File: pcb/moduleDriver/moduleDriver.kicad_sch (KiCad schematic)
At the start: 32 parts, among them J1 MOTOR, J10 Sensor, J11 Power, J12 Power, J2 MOTOR, J3 MOTOR, J4 MOTOR, J7 Sensor, J8 Sensor, J9 Sensor, U5 PicoW

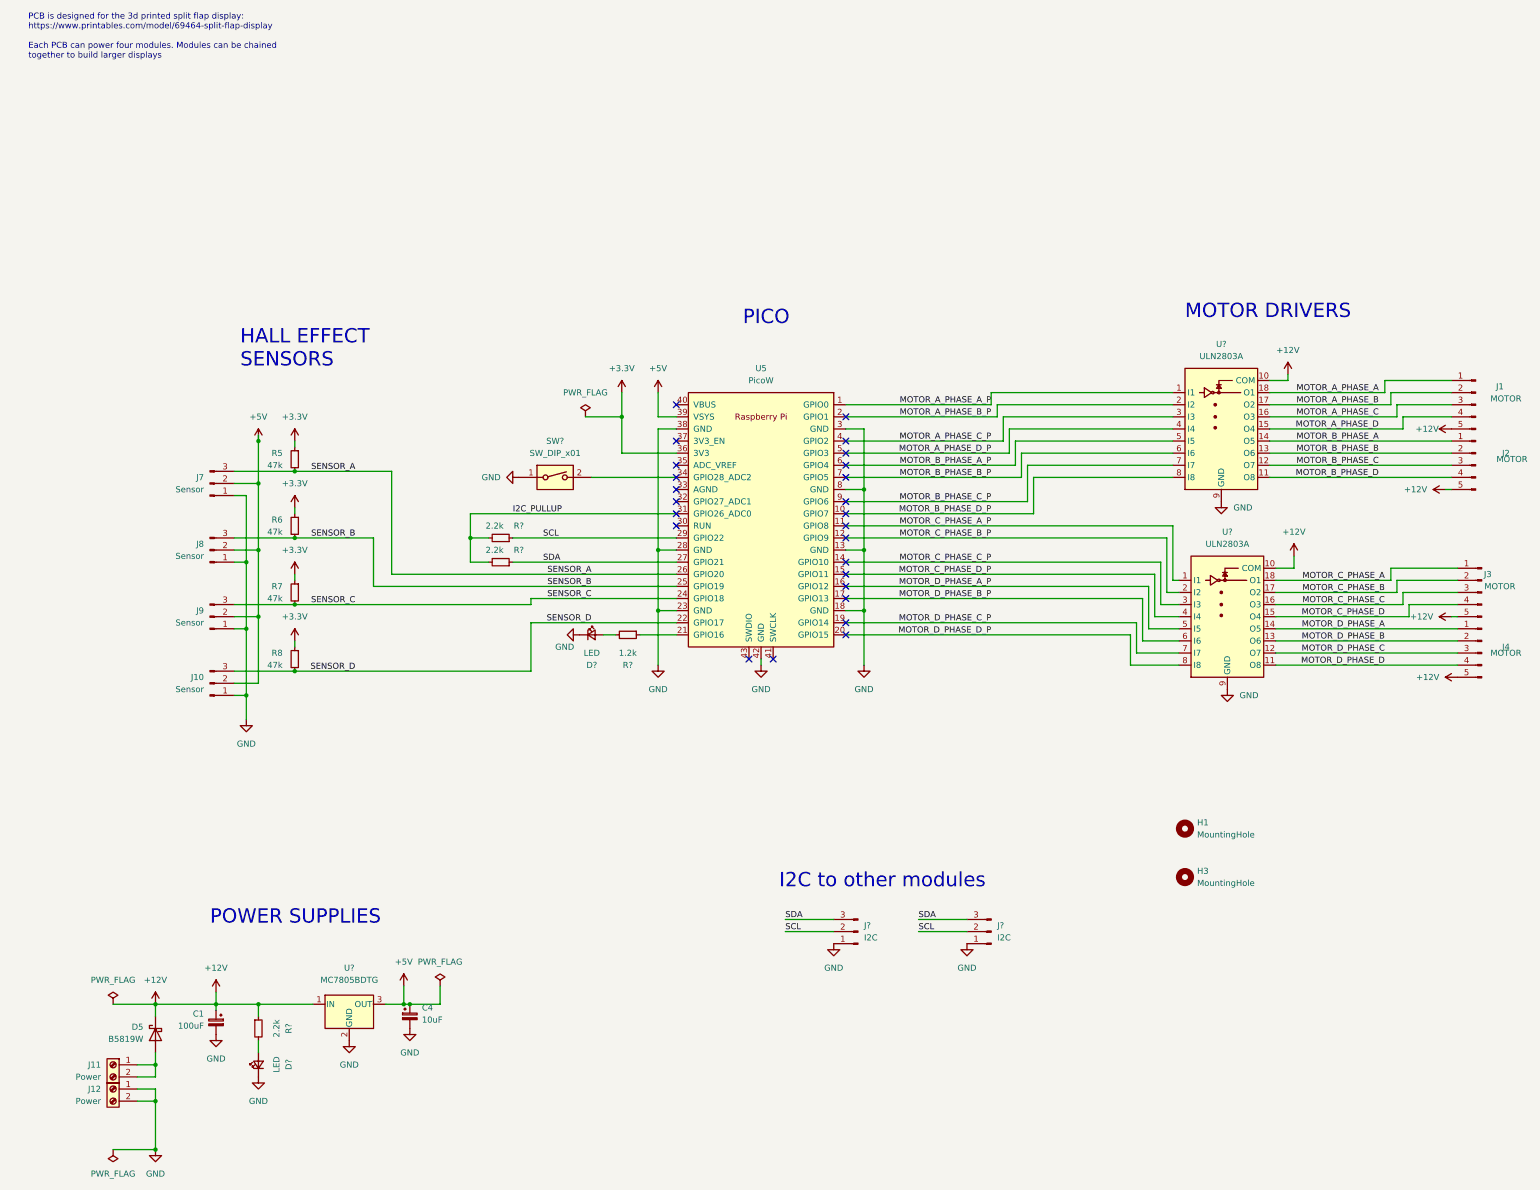
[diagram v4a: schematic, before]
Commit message: cleaned up schematic
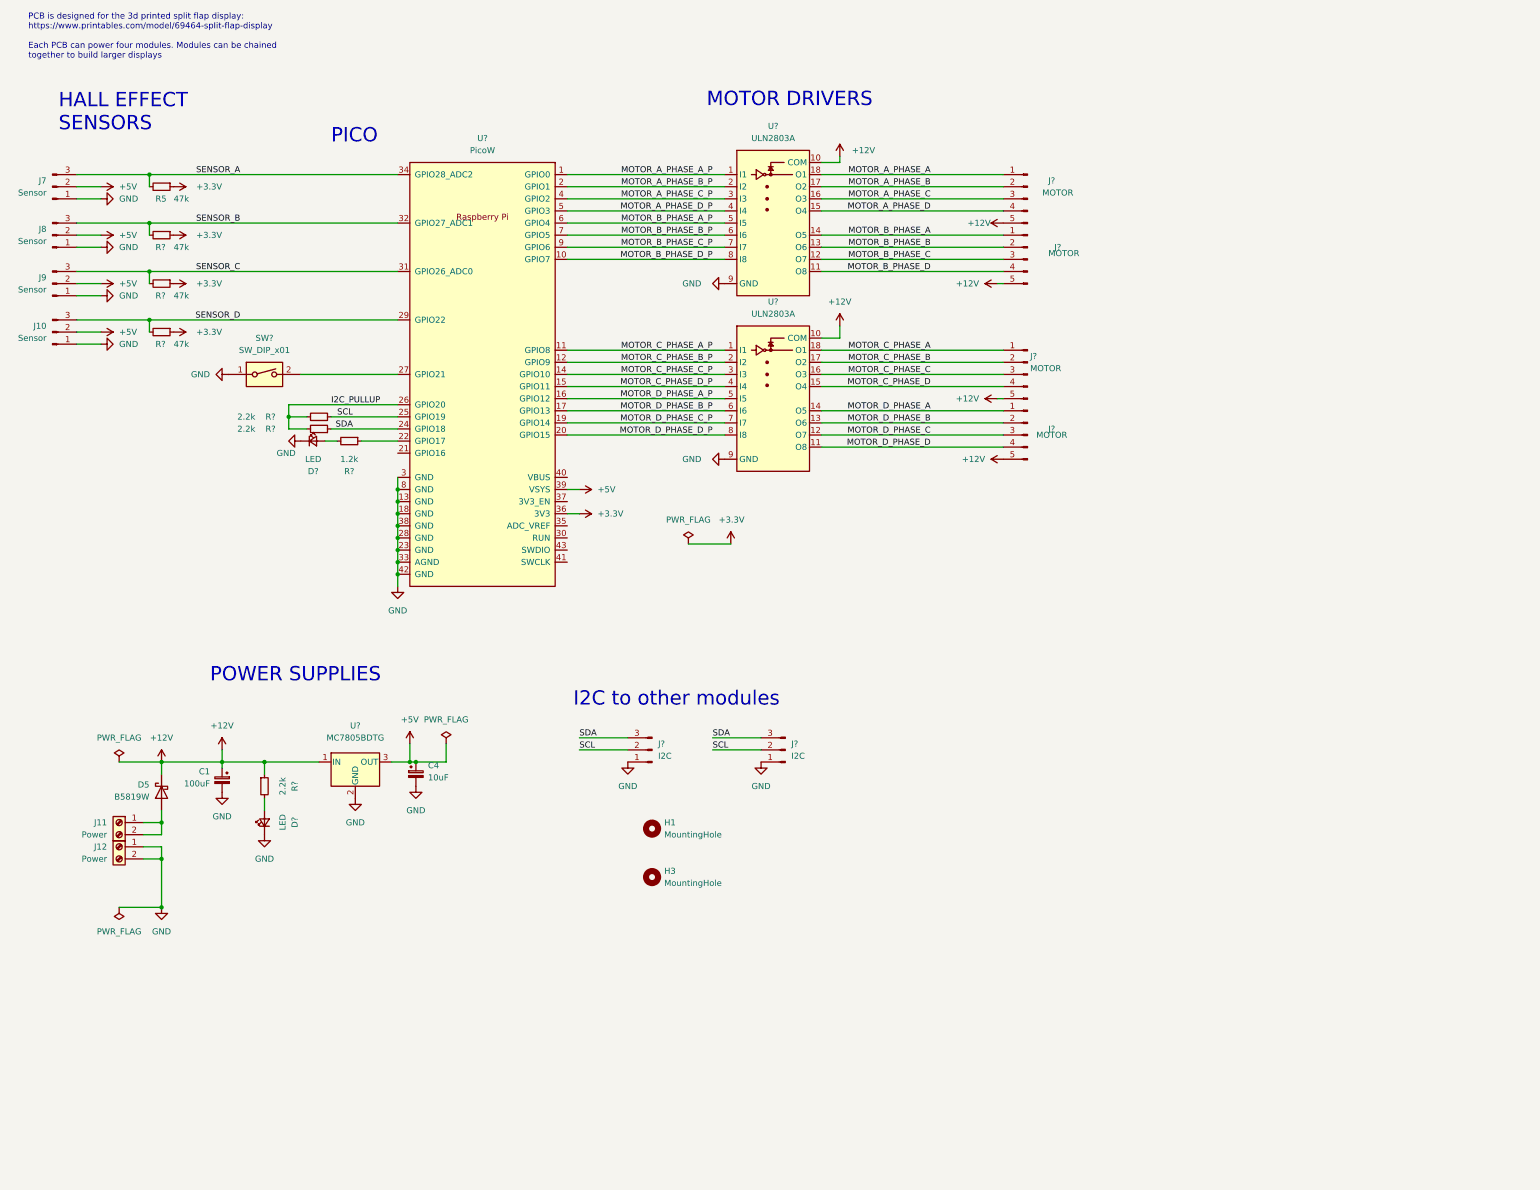
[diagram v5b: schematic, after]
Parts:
- removed J1, J2, J3, J4: MOTOR, Connector_JST:JST_XH_B5B-XH-A_1x05_P2.50mm_Vertical, symbol Connector:Conn_01x05_Male
- removed R6, R7, R8: 47k, Resistor_SMD:R_0603_1608Metric, symbol Device:R_Small
- removed R? (x2): 2.2k, Resistor_SMD:R_0603_1608Metric, symbol Device:R_Small
- removed SW?: SW_DIP_x01, symbol Switch:SW_DIP_x01
- removed U5: PicoW, Library:RPi_PicoW_SMD_TH, symbol RPi_Pico:PicoW
- removed U? (x2): ULN2803A, symbol Transistor_Array:ULN2803A
- added J? (x4): MOTOR, Connector_JST:JST_XH_B5B-XH-A_1x05_P2.50mm_Vertical, symbol Connector:Conn_01x05_Male
- added R? (x2): 2.2k, Resistor_SMD:R_0603_1608Metric, symbol Device:R_Small
- added R? (x3): 47k, Resistor_SMD:R_0603_1608Metric, symbol Device:R_Small
- added SW?: SW_DIP_x01, symbol Switch:SW_DIP_x01
- added U?: PicoW, Library:RPi_PicoW_SMD_TH, symbol RPi_Pico:PicoW
- added U? (x2): ULN2803A, symbol Transistor_Array:ULN2803A
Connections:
- net +12V: now also J?.5 (Pin_5), J?.5 (Pin_5), J?.5 (Pin_5), J?.5 (Pin_5), U?.10 (COM), U?.10 (COM)
- net +3.3V: now also R?.1, R?.1, R?.1, U?.36 (3V3)
- net +5V: now also U?.39 (VSYS)
- net GND: now also SW?.1, U?.13 (GND), U?.18 (GND), U?.23 (GND), U?.28 (GND), U?.3 (GND), U?.33 (AGND), U?.38 (GND), U?.42 (GND), U?.8 (GND), U?.9 (GND), U?.9 (GND)
- net I2C_PULLUP: now also R?.2, R?.2, U?.26 (GPIO20)
- net MOTOR_A_PHASE_A: now also J?.1 (Pin_1), U?.18 (O1)
- net MOTOR_A_PHASE_A_P: now also U?.1 (GPIO0), U?.1 (I1)
- net MOTOR_A_PHASE_B: now also J?.2 (Pin_2), U?.17 (O2)
- net MOTOR_A_PHASE_B_P: now also U?.2 (GPIO1), U?.2 (I2)
- net MOTOR_A_PHASE_C: now also J?.3 (Pin_3), U?.16 (O3)
- net MOTOR_A_PHASE_C_P: now also U?.3 (I3), U?.4 (GPIO2)
- net MOTOR_A_PHASE_D: now also J?.4 (Pin_4), U?.15 (O4)
- net MOTOR_A_PHASE_D_P: now also U?.4 (I4), U?.5 (GPIO3)
- net MOTOR_B_PHASE_A: now also J?.1 (Pin_1), U?.14 (O5)
- net MOTOR_B_PHASE_A_P: now also U?.5 (I5), U?.6 (GPIO4)
- net MOTOR_B_PHASE_B: now also J?.2 (Pin_2), U?.13 (O6)
- net MOTOR_B_PHASE_B_P: now also U?.6 (I6), U?.7 (GPIO5)
- net MOTOR_B_PHASE_C: now also J?.3 (Pin_3), U?.12 (O7)
- net MOTOR_B_PHASE_C_P: now also U?.7 (I7), U?.9 (GPIO6)
- net MOTOR_B_PHASE_D: now also J?.4 (Pin_4), U?.11 (O8)
- net MOTOR_B_PHASE_D_P: now also U?.10 (GPIO7), U?.8 (I8)
- net MOTOR_C_PHASE_A: now also J?.1 (Pin_1), U?.18 (O1)
- net MOTOR_C_PHASE_A_P: now also U?.1 (I1), U?.11 (GPIO8)
- net MOTOR_C_PHASE_B: now also J?.2 (Pin_2), U?.17 (O2)
- net MOTOR_C_PHASE_B_P: now also U?.12 (GPIO9), U?.2 (I2)
- net MOTOR_C_PHASE_C: now also J?.3 (Pin_3), U?.16 (O3)
- net MOTOR_C_PHASE_C_P: now also U?.14 (GPIO10), U?.3 (I3)
- net MOTOR_C_PHASE_D: now also J?.4 (Pin_4), U?.15 (O4)
- net MOTOR_C_PHASE_D_P: now also U?.15 (GPIO11), U?.4 (I4)
- net MOTOR_D_PHASE_A: now also J?.1 (Pin_1), U?.14 (O5)
- net MOTOR_D_PHASE_A_P: now also U?.16 (GPIO12), U?.5 (I5)
- net MOTOR_D_PHASE_B: now also J?.2 (Pin_2), U?.13 (O6)
- net MOTOR_D_PHASE_B_P: now also U?.17 (GPIO13), U?.6 (I6)
- net MOTOR_D_PHASE_C: now also J?.3 (Pin_3), U?.12 (O7)
- net MOTOR_D_PHASE_C_P: now also U?.19 (GPIO14), U?.7 (I7)
- net MOTOR_D_PHASE_D: now also J?.4 (Pin_4), U?.11 (O8)
- net MOTOR_D_PHASE_D_P: now also U?.20 (GPIO15), U?.8 (I8)
- net SCL: now also R?.1, U?.25 (GPIO19)
- net SDA: now also R?.1, U?.24 (GPIO18)
- net SENSOR_A: now also U?.34 (GPIO28_ADC2)
- net SENSOR_B: now also R?.2, U?.32 (GPIO27_ADC1)
- net SENSOR_C: now also R?.2, U?.31 (GPIO26_ADC0)
- net SENSOR_D: now also R?.2, U?.29 (GPIO22)
- net at R?.1: now also U?.22 (GPIO17)
- new net: SW?.2, U?.27 (GPIO21)
- no-connect marks 25 -> 0
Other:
- moved on the sheet: C1, C4, D5, D?, H1, H3, J10, J11, J12, J7, J8, J9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

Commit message: added a couple comments
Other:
- note added: "MASTER SELECT"
- note added: "The switch is to tell which module is the master module. One switch should be ON, and all others OFF. The master module will turn on GPIO20 (I2C_PULLUP), to power the I2C bus. All other modules will have I2C_PULLUP in a High-Z state"
- moved on the sheet: J12
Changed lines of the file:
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@@
   (junction (at 105.41 181.61) (diameter 0) (color 0 0 0 0)
   )
+  (junction (at 53.34 204.47) (diameter 0) (color 0 0 0 0)
+  )
   (junction (at 106.68 181.61) (diameter 0) (color 0 0 0 0)
   )
@@
   (junction (at 102.87 134.62) (diameter 0) (color 0 0 0 0)
   )
-  (junction (at 53.34 201.93) (diameter 0) (color 0 0 0 0)
-  )
   (wire (pts (xy 90.17 114.3) (xy 87.63 114.3))
     (stroke (width 0) (type default) (color 0 0 0 0))
@@
     (stroke (width 0) (type default) (color 0 0 0 0))
   )
-  (wire (pts (xy 53.34 199.39) (xy 53.34 201.93))
-    (stroke (width 0) (type default) (color 0 0 0 0))
-  )
   (wire (pts (xy 80.01 106.68) (xy 102.87 106.68))
     (stroke (width 0) (type default) (color 0 0 0 0))
@@
     (stroke (width 0) (type default) (color 0 0 0 0))
   )
+  (wire (pts (xy 53.34 204.47) (xy 53.34 212.09))
+    (stroke (width 0) (type default) (color 0 0 0 0))
+  )
   (wire (pts (xy 191.77 76.2) (xy 229.87 76.2))
     (stroke (width 0) (type default) (color 0 0 0 0))
@@
     (stroke (width 0) (type default) (color 0 0 0 0))
   )
-  (wire (pts (xy 53.34 201.93) (xy 53.34 212.09))
-    (stroke (width 0) (type default) (color 0 0 0 0))
-  )
   (wire (pts (xy 88.9 111.76) (xy 102.87 111.76))
     (stroke (width 0) (type default) (color 0 0 0 0))
@@
     (stroke (width 0) (type default) (color 0 0 0 0))
   )
-  (wire (pts (xy 53.34 201.93) (xy 49.53 201.93))
+  (wire (pts (xy 53.34 204.47) (xy 49.53 204.47))
     (stroke (width 0) (type default) (color 0 0 0 0))
   )
@@
     (stroke (width 0) (type default) (color 0 0 0 0))
   )
-  (wire (pts (xy 49.53 199.39) (xy 53.34 199.39))
+  (wire (pts (xy 49.53 201.93) (xy 53.34 201.93))
+    (stroke (width 0) (type default) (color 0 0 0 0))
+  )
+  (wire (pts (xy 53.34 204.47) (xy 53.34 201.93))
     (stroke (width 0) (type default) (color 0 0 0 0))
   )
@@
   (wire (pts (xy 35.56 73.66) (xy 40.64 73.66))
     (stroke (width 0) (type default) (color 0 0 0 0))
+  )
+  (text "The switch is to tell which module\nis the master module. One switch\nshould be ON, and all others OFF.\n\nThe master module will turn on GPIO20\n(I2C_PULLUP), to power the I2C bus.  \nAll other modules will have I2C_PULLUP\nin a High-Z state"
+    (at 24.13 119.38 0)
+    (effects (font (size 1.27 1.27)) (justify left bottom))
   )
   (text "HALL EFFECT\nSENSORS" (at 31.75 49.53 0)
@@
   )
   (text "PICO" (at 88.9 52.07 0)
+    (effects (font (size 3 3)) (justify left bottom))
+  )
+  (text "MASTER SELECT" (at 24.13 101.6 0)
     (effects (font (size 3 3)) (justify left bottom))
   )
@@
     (pin "1")
   )
-  (symbol (lib_id "Connector:Screw_Terminal_01x02") (at 44.45 199.39 0) (mirror y) (unit 1)
-    (in_bom yes) (on_board yes) (fields_autoplaced)
-    (property "Reference" "J12" (id 0) (at 41.91 199.3899 0)
+  (symbol (lib_id "Connector:Screw_Terminal_01x02") (at 44.45 201.93 0) (mirror y) (unit 1)
+    (in_bom yes) (on_board yes) (fields_autoplaced)
+    (property "Reference" "J12" (id 0) (at 41.91 201.9299 0)
       (effects (font (size 1.27 1.27)) (justify left))
     )
-    (property "Value" "Power" (id 1) (at 41.91 201.9299 0)
+    (property "Value" "Power" (id 1) (at 41.91 204.4699 0)
       (effects (font (size 1.27 1.27)) (justify left))
     )
-    (property "Footprint" "Library:ScrewTerminal-5.08-2P" (id 2) (at 44.45 199.39 0)
-      (effects (font (size 1.27 1.27)) hide)
-    )
-    (property "Datasheet" "~" (id 3) (at 44.45 199.39 0)
-      (effects (font (size 1.27 1.27)) hide)
-    )
-    (property "Comment" "-" (id 4) (at 44.45 199.39 0)
-      (effects (font (size 1.27 1.27)) hide)
-    )
+    (property "Footprint" "Library:ScrewTerminal-5.08-2P" (id 2) (at 44.45 201.93 0)
+      (effects (font (size 1.27 1.27)) hide)
+    )
+    (property "Datasheet" "~" (id 3) (at 44.45 201.93 0)
+      (effects (font (size 1.27 1.27)) hide)
+    )
+    (property "Comment" "-" (id 4) (at 44.45 201.93 0)
+      (effects (font (size 1.27 1.27)) hide)
+    )

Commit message: update more text
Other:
- note added: "As you're laying out, double click the pico and click edit symbol. Then swap around all the GPIOs to make routing easier. Except for the I2C bus, literally all the GPIOS are interchangeable. Make routing simple."
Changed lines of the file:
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@@
     (effects (font (size 3 3)) (justify left bottom))
+  )
+  (text "As you're laying out, double click the pico and click\nedit symbol.  Then swap around all the GPIOs to make \nrouting easier.  Except for the I2C bus, literally\nall the GPIOS are interchangeable.  Make routing simple."
+    (at 102.87 41.91 0)
+    (effects (font (size 1.27 1.27)) (justify left bottom))
   )
   (text "MASTER SELECT" (at 24.13 101.6 0)
